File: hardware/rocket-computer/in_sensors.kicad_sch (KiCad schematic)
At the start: 16 parts, among them J1 BM05B-SRSS-TB, Q1 PMPB14XNX, U2 ISM6HG256XTR, U3 IIS2MDCTR, U4 BMP585

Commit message: hardware: MPN + Mfr on every purchased part of the three ESP32 boards
Closes the LoRa pre-fab review's finding 3, extended to the sibling boards.
Every non-DNP symbol now names the exact part the cross-board BOM prices, so
the schematic can no longer imply a part that was never quoted.

401 of 401 purchasable parts carry an MPN. The only exemptions are the three
DNP v3.x provisions on the rocket-computer (R74/R75 499 k, R76 0 R): not
fitted, so never purchased, so correctly absent from the BOM.

Values normalised so each part resolves to one BOM line:

  LoRa R74  "10 K" -> "10 k"   capital K split one part across two lines
  LoRa D6   "LED"  -> "Green"  no colour recorded, so no MPN could attach
  Y1/Y3/Y5  "SC-32S-32.768kHz-12.5pF" -> "ABS07-32.768KHZ-T"

Two stale legacy MP fields disagreed with both the Value and the BOM and were
corrected -- a symbol carrying two part numbers is the wrong-part-order hazard
this pass exists to remove:

  rocket U19  TPS259824LNRGER -> ...RGET.  Same die and RGE-24 package; the
              suffix is reel quantity, and power-eco.md documents RGET.
  base   U9   TPS63021DSJR -> TPS63020DSJR.  These are NOT interchangeable:
              63021 is fixed 3.3 V, 63020 is adjustable. U9 pin 3 (FB) drives
              a real divider (R13 1 M / R16 180 k -> 0.5 x (1 + 1M/180k) =
              3.28 V), which only the adjustable part uses. BOM was right.

The ABS07 keeps the existing XTAL_SC-32S_3215 footprint: both parts are
2-pad 3.2 x 1.5 mm tuning forks, so the land is correct and only the
footprint's name now reads for the superseded vendor.

ERC clean on all three boards after the pass.

Co-Authored-By: Claude Opus 5 <noreply@anthropic.com>
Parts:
- C2: MPN (none) -> CL05B104KO5NNNC; Mfr (none) -> Samsung
- C3, C4, C5: MPN (none) -> CL05A106MQ5NUNC; Mfr (none) -> Samsung
- C6: MPN (none) -> CL05B224KO5NNNC; Mfr (none) -> Samsung
- C7: MPN (none) -> CL21A226MOQNNNE; Mfr (none) -> Samsung
- FL1: MPN (none) -> BLM18PG471SN1D; Mfr (none) -> Murata
- J1: MPN (none) -> BM05B-SRSS-TB; Mfr (none) -> JST
- Q1: MPN (none) -> PMPB14XNX; Mfr (none) -> Nexperia
- R4, R5, R7: MPN (none) -> RC0402FR-0710KL; Mfr (none) -> Yageo
- R6: MPN (none) -> RC0402FR-071KL; Mfr (none) -> Yageo
- U2: MPN (none) -> ISM6HG256XTR; Mfr (none) -> STMicro
- U3: MPN (none) -> IIS2MDCTR; Mfr (none) -> STMicro
- U4: MPN (none) -> BMP585; Mfr (none) -> Bosch

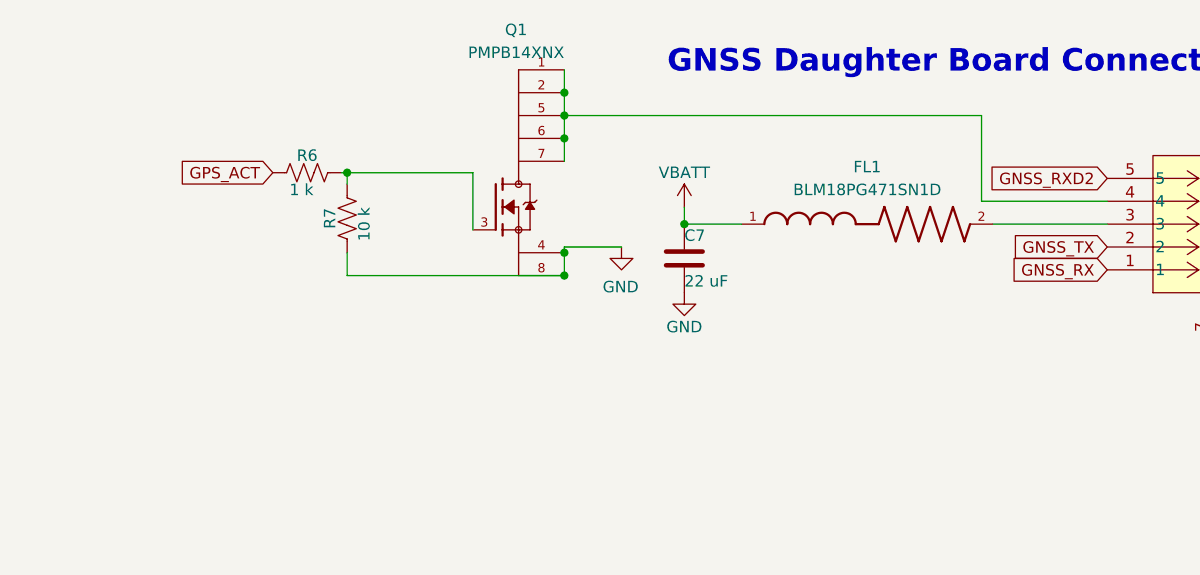
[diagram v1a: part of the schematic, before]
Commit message: hardware(rocket-computer): V9 pre-fab review close-out -- every finding fixed, measured, or waived
Closes the 2026-08-04..09 pre-manufacturing review (170 raw findings).
WORKLIST.md is the closing record: D-1..D-4 decided, H-1..H-10 and
M-1..M-25 dispositioned, Lows annotated, bench list is the remainder.

Power architecture:
- All four peripheral branches converted low-side N-FET -> integrated
  high-side switches (U26/U28 TPS22811LRPWR, U27/U29 TPS22810DRVR);
  U30 TPS22810DRVR gates the P4 domain. Every connector ground is now
  hard GND; the 12 EXP lines stay resistor-free by design (H-3/D-4).
  J3 and J4 power pins swapped ends -- fab notes B6/B7 carry the
  harness warnings.
- Q11 (CSD25404Q3) reverse-polarity P-FET at the battery input on a
  new TI-pattern footprint; CR2 re-purposed as connector ESD clamp
  upstream of it (M-9/M-10). Kelvin sense at R72 preserved.
- P4 rail self-latch: D9 (BAV170M) OR-gates S3 request with P4 hold,
  C105 rides the P4 through its own reset (H-4; firmware in #718).
- eFuse UVLO deglitch C94 (H-1); brownout decided as clean-reboot,
  ECO hold-up claims corrected in power-eco.md (H-8/D-3).
- Pyro gate-drive stiffened: R22 -> 5.11k, R78-R81 shunts (H-2).
- Servo budget decided at 3 A set by the In2 stretch; ILIM left open
  at 11.6 A; SERVO_IMON flight data gates any increase (D-1).

Component and BOM:
- TPS2121 ILIM 18.7k -> 49.9k (real protection at 2.26 A typ, M-5).
- IMON scaling: R85 -> 2.2k (3 A camera), R88 -> 1k (servo open).
- C27 VDD_SPI 10u -> 1u per HDG (M-4); switch VIN bypass 100n -> 1u;
  C40/C76 consolidation; C65 MPN fixed (was a 390 pF part number
  under a 100 nF value -- would have misassembled the buck bypass).
- SW2/SW3 on the R-667995 tact switch, footprint imported and pads
  renumbered to match; FB-network DNP parts carry MPNs for the v3.x
  flip (M-22); bom.csv regenerated: 79 lines / 243 placements, every
  part carries an MPN. Priced BOMs evicted from board dirs (they live
  in Documents/Circuit Board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
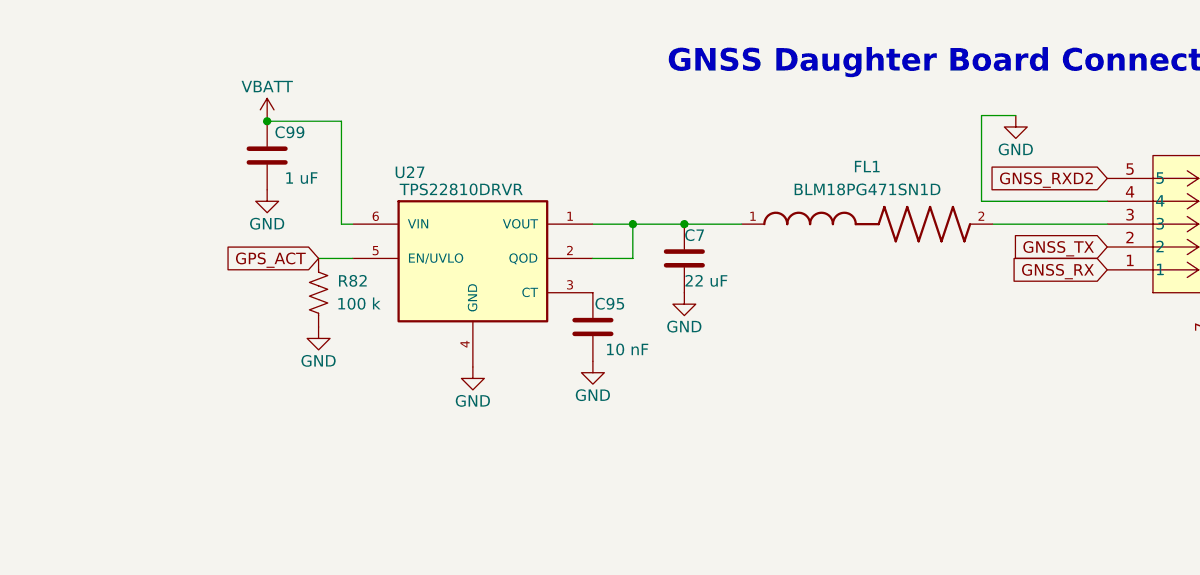
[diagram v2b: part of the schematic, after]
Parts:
- removed Q1: PMPB14XNX, Footprints:TRANS_PMPB14XNX, symbol Custom:PMPB14XNX
- removed R6: 1 k, Resistor_SMD:R_0402_1005Metric, symbol Device:R_US
- removed R7: 10 k, Resistor_SMD:R_0402_1005Metric, symbol Device:R_US
- added C95: 10 nF, Capacitor_SMD:C_0402_1005Metric, symbol Device:C
- added C99: 1 uF, Capacitor_SMD:C_0402_1005Metric, symbol Device:C
- added R82: 100 k, Resistor_SMD:R_0402_1005Metric, symbol Device:R_US
- added U27: TPS22810DRVR, Footprints:SON65P200X200X80-7N, symbol Custom:TPS22810DRVR
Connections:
- net GND: now also J1.4, C95.2, C99.2, R82.2, U27.4 (GND), U27.7 (GND)
- net GPS_ACT: now also R82.1, U27.5 (EN/UVLO)
- net VBATT: now also C99.1, U27.6 (VIN); no longer C7.1, FL1.1
- new net: C7.1, FL1.1, U27.1 (VOUT), U27.2 (QOD)
- new net: C95.1, U27.3 (CT)

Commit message: hardware(rocket-computer): correct R85/R88 MPNs to their reworked values; Samsung Mfr on the 10 nF group
R85 (2.2 k, camera IMON) and R88 (1 k, servo IMON) still carried the
3.3 k Yageo code from before the IMON rework -- order-and-misassemble
class, caught by the priced-BOM refresh. C95/C96/C97/C101/C104 get
their Mfr field so BOM lines cannot split. Audited all 75 Yageo
RC0402 parts value-vs-code: zero mismatches remain. bom.csv
regenerated; Documents snapshot updated.

Co-Authored-By: Claude Fable 5 <noreply@anthropic.com>
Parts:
- C95: Mfr (none) -> Samsung
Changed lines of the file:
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@@
 			)
+		)
+		(property "Mfr" "Samsung"
+			(at 0 0 0)
+			(hide yes)
+			(show_name no)
+			(do_not_autoplace no)
+			(effects (font (size 1.27 1.27)))
 		)
 		(property "Datasheet" ""

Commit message: hardware(V10): the #678 sweep — NRETRY to ground, LEDs at 1 k, H2 grounded, the missing bypasses, and the U9 pin-9 parity fix (#1360)
Schematic, library and BOM only; the board is untouched. Record:
hardware/rocket-computer/v10-power-parity-2026-09-11.md section 6.4.

## Owner decisions (2026-09-11)

- NRETRY to ground: C45 (1 uF, ~1800 retries, past the datasheet's last
  quantization bucket) deleted, U19 pin 11 tied to GND. With C46 2.2 nF
  still on RETRY_DLY the TPS25982 fault table reads "auto-retry
  indefinitely with finite delay" -- a finite count ends in latch-off,
  which a flight computer must never do.
- Status LEDs: R65, R66, R70 10 k -> 1 k (stocked line). ~1.5 mA green,
  ~1.3 mA red, ~0.4 mA blue instead of 0.05-0.15 mA.
- H2, the plated mounting ring 0.6 mm from the antenna body, on no net:
  H2 becomes Mechanical:MountingHole_Pad with pin 1 on GND. The other
  seven holes are unchanged; the pad's zone connection is the layout
  pass's.

## Simple adds from the same list

- C44 soft-start 390 pF -> 10 nF (the buck started in current limit into
  its output capacitance; ~5 ms now, datasheet class).
- R141 10 k pull-up on S3 GPIO0 to +3V3, on the wire to the boot button.
- C146 / C147 100 nF at the IMU and baro VDD pins (their nearest 100 nF
  was the magnetometer's at 3-4 mm), on V_MCU_SWTCH.
- C148 10 uF on the S3 RF supply net, converter side of L4 (the guide
  asks 10 uF per RF pin; there was only C33 100 nF).
- ISM6HG256_INT2: single-pin label replaced by a no-connect flag.
- U9 CSD16323Q3 symbol pin 9 renumbered 5 in Custom.kicad_sym and in the
  cached copies on this board and the mini: the shared TSON footprint
  numbers its drain tab as a second pad 5, so the symbol now matches it
  and the permanent "no pad for pin 9" parity warning is gone on both
  boards. Netlists unchanged.
- power-eco.md Change 2 pin table rewritten to the as-built designators
  and values (ITIMER/dVdt/NRETRY had drifted; the input clamp is gone).

Not changed, recorded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
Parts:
- added C146, C147: 100 nF, Capacitor_SMD:C_0402_1005Metric, symbol Device:C
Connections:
- net GND: now also C146.2, C147.2
- net V_MCU_SWTCH: now also C146.1, C147.1
- net ISM6HG256_INT2: no longer names the net of U2.9 (INT2)
- no-connect marks 2 -> 3

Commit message: rocket-computer: the voltage/current measurement block moves to the sensors sheet (#1374)
The INA230 and its shunt are telemetry, not power conversion, so the block
leaves `power.kicad_sch` for `in_sensors.kicad_sch`. Nothing electrical
changes: every connection the block makes to the rest of the design is a
global label or a power symbol, so the move is a pure translation.

Moved, 38 entities offset by (-48.26, +55.88) mm — a multiple of 1.27, so
the block stays on grid:

- U23 (INA230AIRGTR) and R72, the 2 mOhm shunt
- R67 / R69, the PWR_SCL / PWR_SDA pull-ups
- R142, the INA_ALERT pull-up — it exists only for U23 pin 3, so it travels
  with the part rather than staying behind on a sheet that no longer has
  anything to alert about
- the six power symbols, 14 wires, 8 global labels, 4 junctions and the
  block title

`Custom:INA230AIRGTR` and `power:+3V3` were added to the Sensors sheet's
`lib_symbols` cache; the INA230 entry left Power's, which nothing there
still uses. Symbol UUIDs are unchanged, so the four placed footprints keep
their position and routing and only their sheet path is rewritten
(`path`, `sheetname`, `sheetfile`). No footprint moved; no track changed.

Also removed from the layout, as three footprints with no symbol behind
them — the board's whole `extra_footprint` parity count:

- C12 and R20, the 10 mF pyro store and its 150 Ohm charge resistor,
  deleted from the schematic in 7ad75086 when the channels went pack-direct
- C45, the NRETRY delay cap, deleted in 501a4e1e when U19 pin 11 went to
  ground

Their copper is left in place: 12 dangling stubs on GND, V_CAP, VBATT and
Net-(U19-NRETRY), and fills that are now stale around the three sites.
Pruning and refilling belong to the V10 layout pass (#1365), not here.

Verified: net membership diff 0 over 241 nets; ERC 982 -> 982 with no
item-level difference; every block that stayed is byte-identical and each
moved block round-trips to an exact byte match when the offset is
subtracted back off; pa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
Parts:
- added R142: 100 k, Resistor_SMD:R_0402_1005Metric, symbol Device:R_US
- added R67, R69: 5.11 k, Resistor_SMD:R_0402_1005Metric, symbol Device:R_US
- added R72: 2 m, Resistor_SMD:R_0805_2012Metric, symbol Device:R_US
- added U23: INA230AIRGTR, Footprints:RGT16_1P7X1P7, symbol Custom:INA230AIRGTR
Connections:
- net GND: now also U23.1 (A1), U23.10 (GND), U23.17 (EPAD), U23.2 (A0)
- new net +3V3: R142.1, R67.1, R69.1, U23.9 (VS+)
- new net INA_ALERT: R142.2, U23.3 (ALERT)
- new net PWR_SCL: R67.2, U23.5 (SCL)
- new net PWR_SDA: R69.2, U23.4 (SDA)
- new net VBAT_CON: R72.1, U23.11 (BUS), U23.12 (IN-)
- new net VBAT_Terminal: R72.2, U23.13 (IN+)
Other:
- note added: "Voltage/Current Measurement"
